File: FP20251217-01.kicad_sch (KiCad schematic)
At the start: 13 parts, among them J1 216-3340-00-0602J, J3 Arduino P2 to P9, J4 Conn_01x02, J5 Arduino A0-A4, Pin 10

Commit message: Roughing out PCB
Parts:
- added J2: Arduino A4, A5, Connector_PinSocket_2.54mm:PinSocket_1x02_P2.54mm_Vertical, symbol Connector_Generic:Conn_01x02
- added J6: Display, Connector_PinSocket_2.54mm:PinSocket_1x04_P2.54mm_Vertical, symbol Connector_Generic:Conn_01x04
- added J7: Read Button, Connector_PinSocket_2.54mm:PinSocket_1x02_P2.54mm_Vertical, symbol Connector_Generic:Conn_01x02
- added J8: Arduino P12, Connector_PinSocket_2.54mm:PinSocket_1x02_P2.54mm_Vertical, symbol Connector_Generic:Conn_01x02
- added R10, R11, R9: 10k, Resistor_THT:R_Axial_DIN0309_L9.0mm_D3.2mm_P12.70mm_Horizontal, symbol Device:R
- J4: value Conn_01x02 -> Arduino Power Supply
- J5: value Arduino A0-A4, Pin 10 -> Arduino A0-A3, Pin 10 & 11
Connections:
- net +5V: now also J6.1 (Pin_1), R10.1, R11.1, R9.1
- net GND: now also J1.7 (O7), J1.9 (O8), J3.7 (Pin_7), J3.8 (Pin_8), R7.2, R8.2, J6.4 (Pin_4), J7.2 (Pin_2), J8.2 (Pin_2)
- net O3: now reaches J1.3 (O3), J3.3 (Pin_3), R3.2
- net O5: now reaches J1.5 (O5), J3.5 (Pin_5), R5.2
- net O1: now reaches J1.1 (O1), J3.1 (Pin_1), R1.2
- net A0: now reaches J1.10 (A0), J5.1 (Pin_1)
- net A1: now reaches J1.11 (A1), J5.2 (Pin_2)
- net A2: now reaches J1.12 (A2), J5.3 (Pin_3)
- net A3: now reaches J1.13 (A3), J5.4 (Pin_4)
- net A4: now reaches J1.14 (A4), J5.5 (Pin_5)
- net ~{CE}: now reaches J1.15 (~{CE}), J5.6 (Pin_6)
- net O2: now reaches J1.2 (O2), J3.2 (Pin_2), R2.2
- net O4: now reaches J1.4 (O4), J3.4 (Pin_4), R4.2
- net O6: now reaches J1.6 (O6), J3.6 (Pin_6), R6.2
- new net PB: J7.1 (Pin_1), J8.1 (Pin_1), R11.2
- new net SCL: J2.2 (Pin_2), J6.3 (Pin_3), R10.2
- new net SDA: J2.1 (Pin_1), J6.2 (Pin_2), R9.2
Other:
- moved on the sheet: C1, J1, J3, J4, J5, R1, R2, R3, R4, R5, R6, R7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

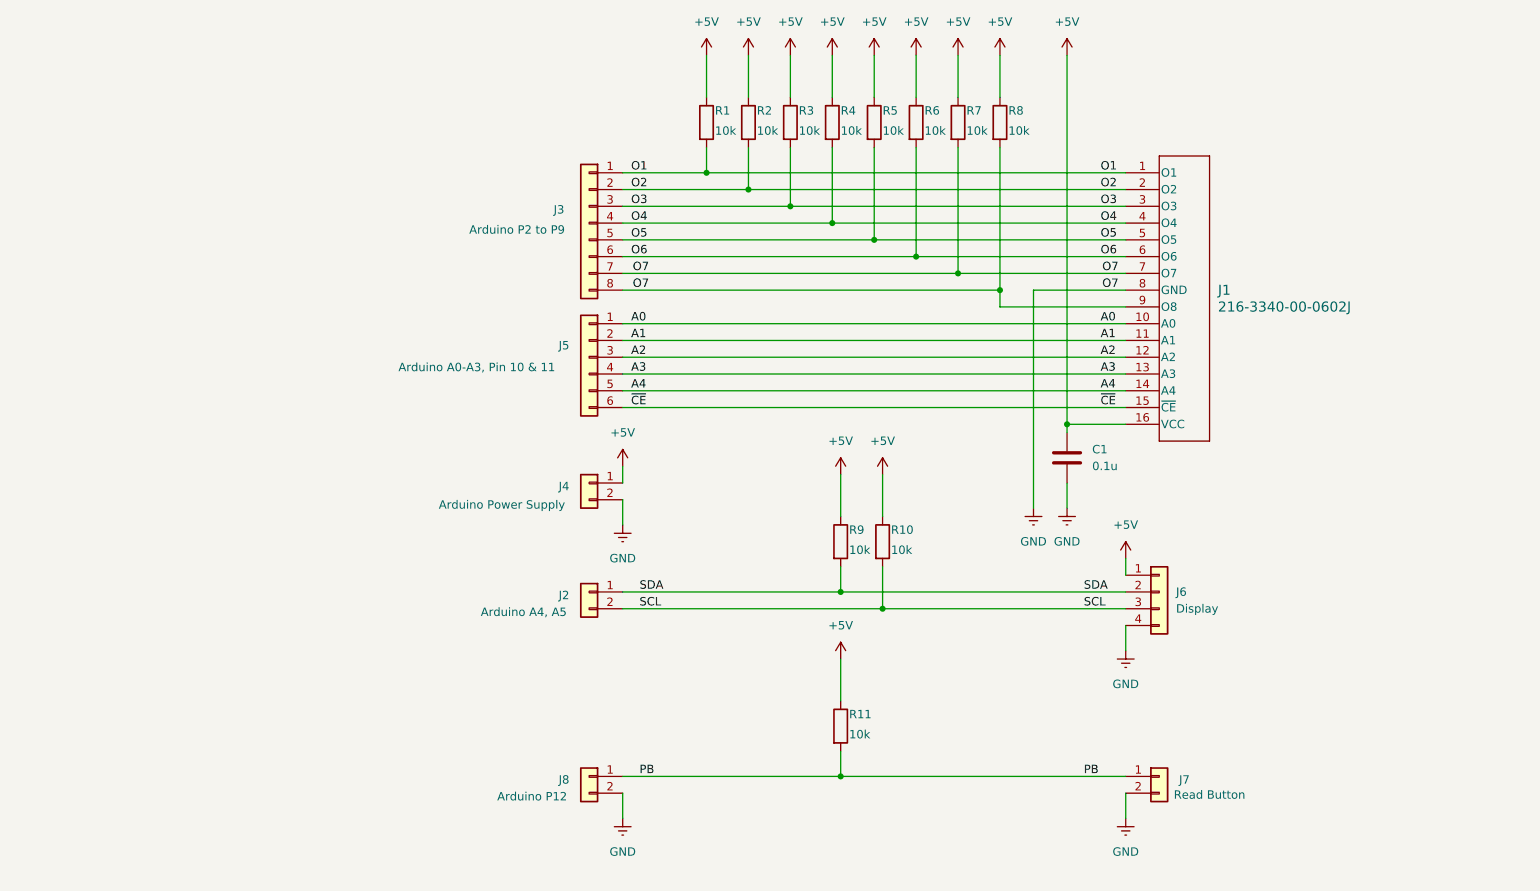
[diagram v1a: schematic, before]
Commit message: Includes arduino module on sch
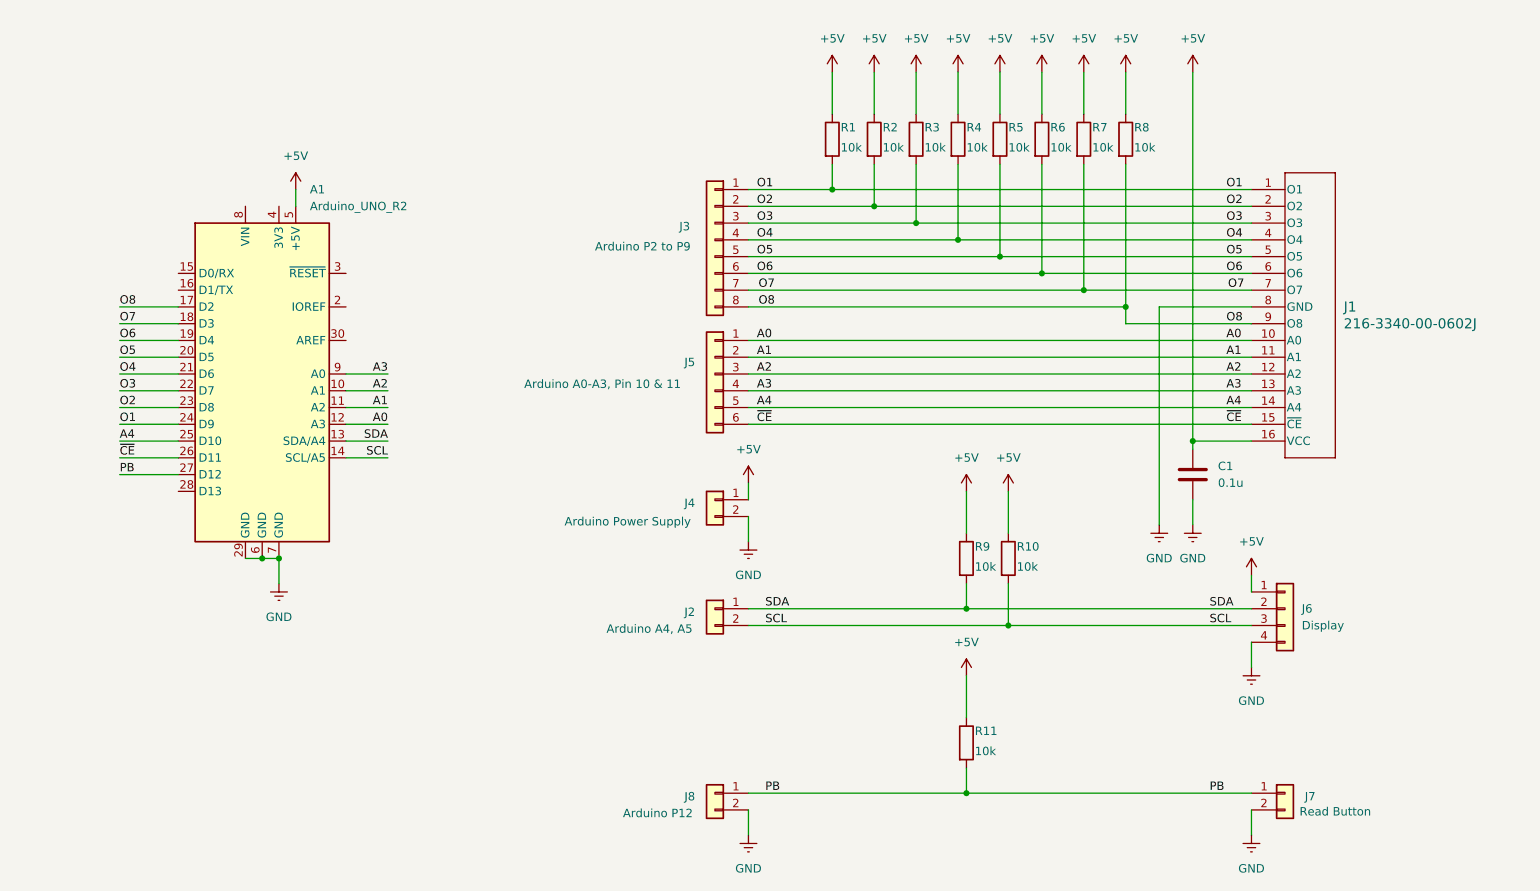
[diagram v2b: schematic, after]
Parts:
- added A1: Arduino_UNO_R2, Module:Arduino_UNO_R2, symbol MCU_Module:Arduino_UNO_R2
- R1, R10, R11, R2, R3, R4, R5, R6, R7, R8, R9: footprint Resistor_THT:R_Axial_DIN0309_L9.0mm_D3.2mm_P12.70mm_Horizontal -> Resistor_THT:R_Axial_DIN0207_L6.3mm_D2.5mm_P10.16mm_Horizontal
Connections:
- net +5V: now also A1.5 (+5V)
- net A0: now also A1.12 (A3)
- net A1: now also A1.11 (A2)
- net A2: now also A1.10 (A1)
- net A3: now also A1.9 (A0)
- net A4: now also A1.25 (D10)
- net GND: now also A1.29 (GND), A1.6 (GND), A1.7 (GND); no longer J1.7 (O7), J1.9 (O8), J3.7 (Pin_7), J3.8 (Pin_8), R7.2, R8.2
- net O1: now also A1.24 (D9)
- net O2: now also A1.23 (D8)
- net O3: now also A1.22 (D7)
- net O4: now also A1.21 (D6)
- net O5: now also A1.20 (D5)
- net O6: now also A1.19 (D4)
- net PB: now also A1.27 (D12)
- net SCL: now also A1.14 (SCL/A5)
- net SDA: now also A1.13 (SDA/A4)
- net ~{CE}: now also A1.26 (D11)
- new net O7: A1.18 (D3), J1.7 (O7), J3.7 (Pin_7), R7.2
- new net O8: A1.17 (D2), J1.9 (O8), J3.8 (Pin_8), R8.2
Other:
- moved on the sheet: C1, J1, J2, J3, J4, J5, J6, J7, J8, R1
